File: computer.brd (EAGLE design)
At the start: 99.9 x 90.2 mm, 74 parts, among them IC2 74HC541N, IC3 74HC573N, IC4 74HC04N, Q1 IRF9530, X1 1503_08

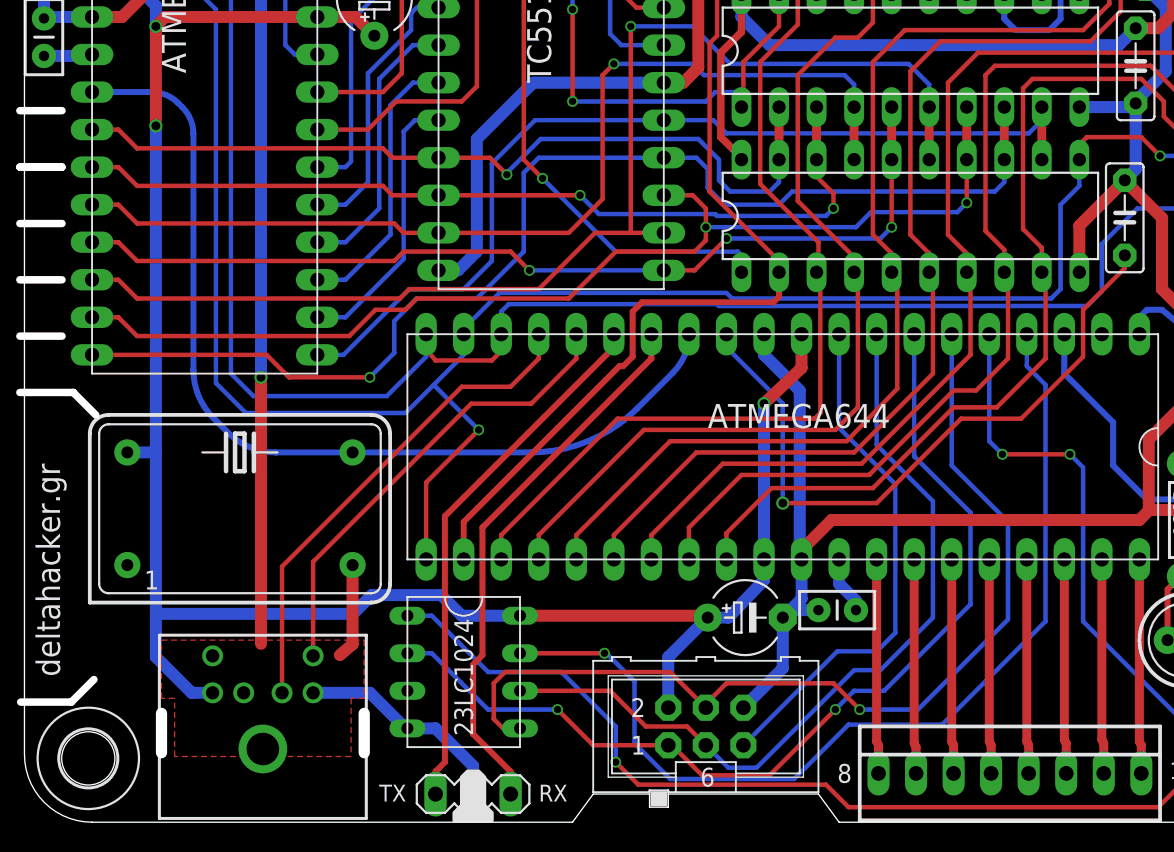
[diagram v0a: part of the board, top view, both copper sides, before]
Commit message: minor modifications (mainly to satisfy my OCD)
Signed-off-by: Panagiotis Varelas <varelaspanos@gmail.com>
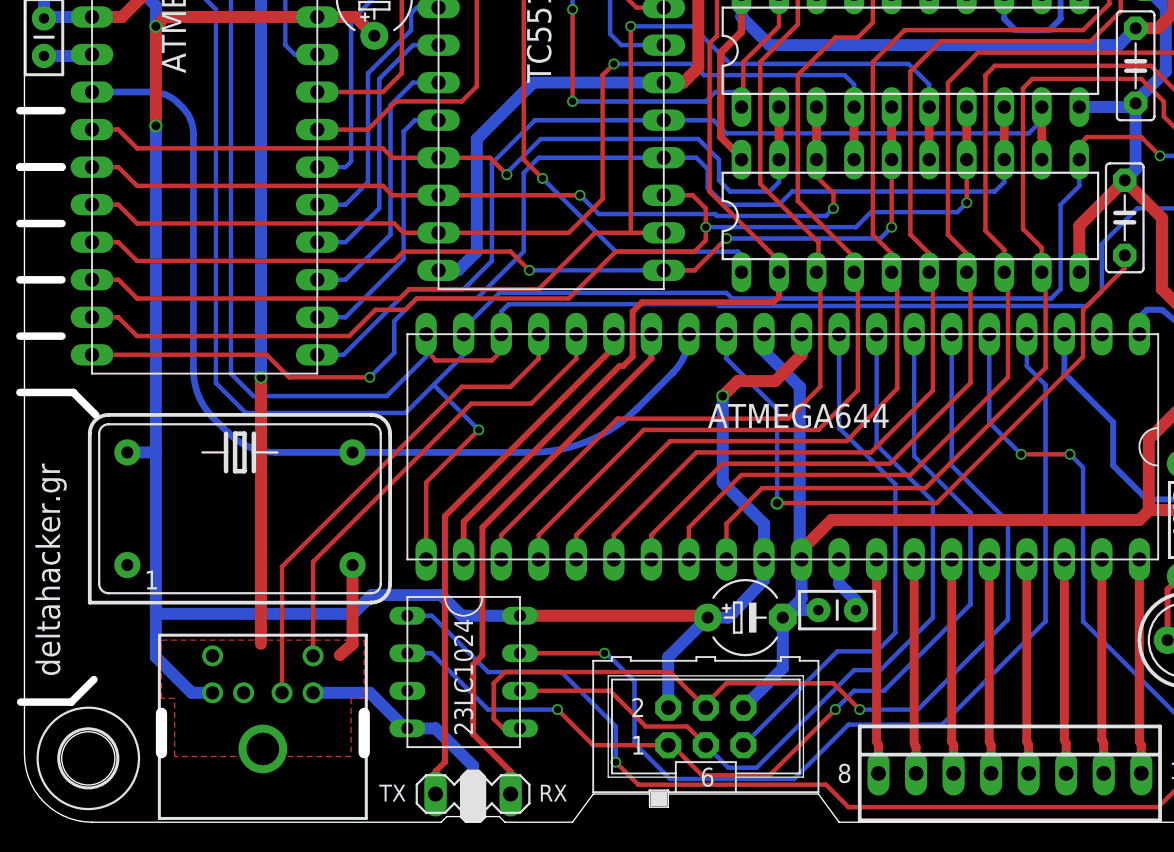
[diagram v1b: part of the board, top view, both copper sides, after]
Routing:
- net VCC: track 358.7 -> 362.5 mm
- net CPUDATA5: track 66.1 -> 67.2 mm
- net CPUDATA1: track 96.5 -> 95.5 mm
- net N$52: track 98.3 -> 97.5 mm
- net CPUDATA7: track 62.3 -> 63.0 mm
- net CPUDATA6: track 64.6 -> 65.4 mm
- net CPUDATA4: track 79.0 -> 79.6 mm
- net CPUDATA2: track 90.2 -> 89.5 mm
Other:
- outline, holes or cut-outs redrawn
- board text added: "Oct 2016"
- board text removed: "2016"
